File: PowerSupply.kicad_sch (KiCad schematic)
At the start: 42 parts, among them Q1 CSD17318Q2, Q2 CSD17318Q2, U1 TPS55288RPMR

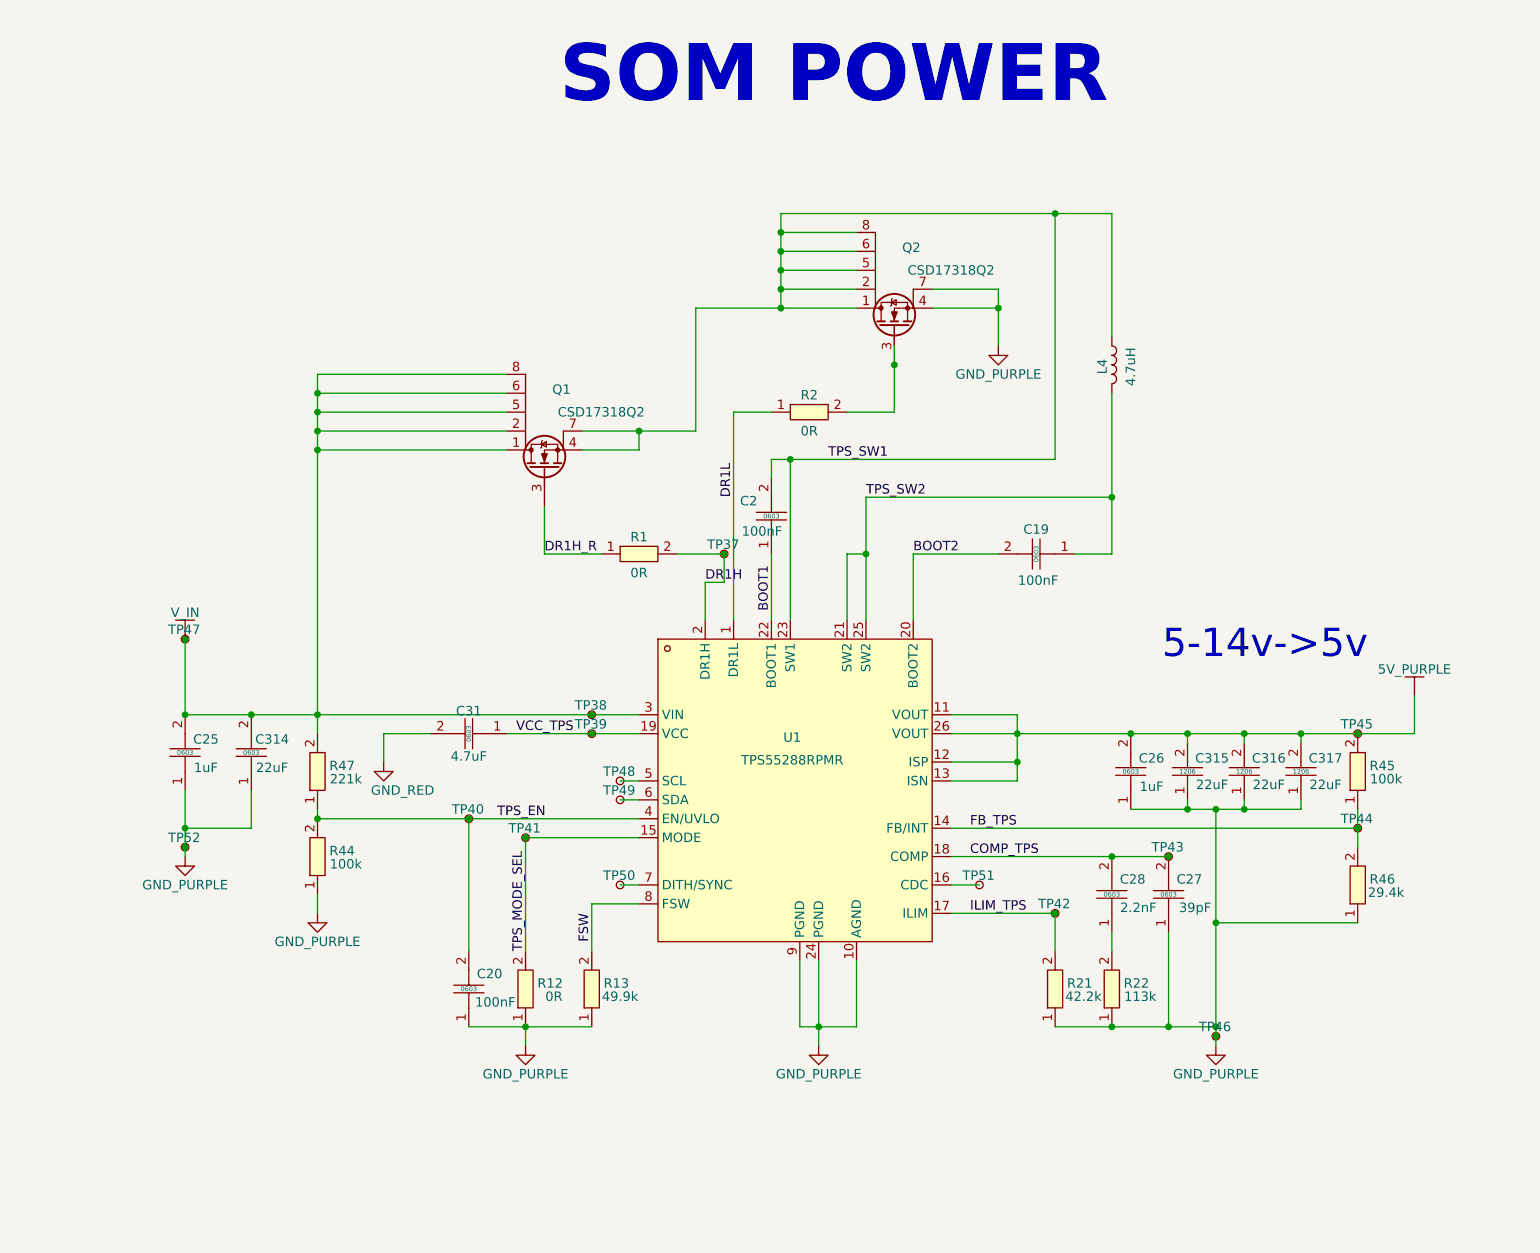
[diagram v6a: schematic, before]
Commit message: Recreate TPS block in KiCad with 0603+ components
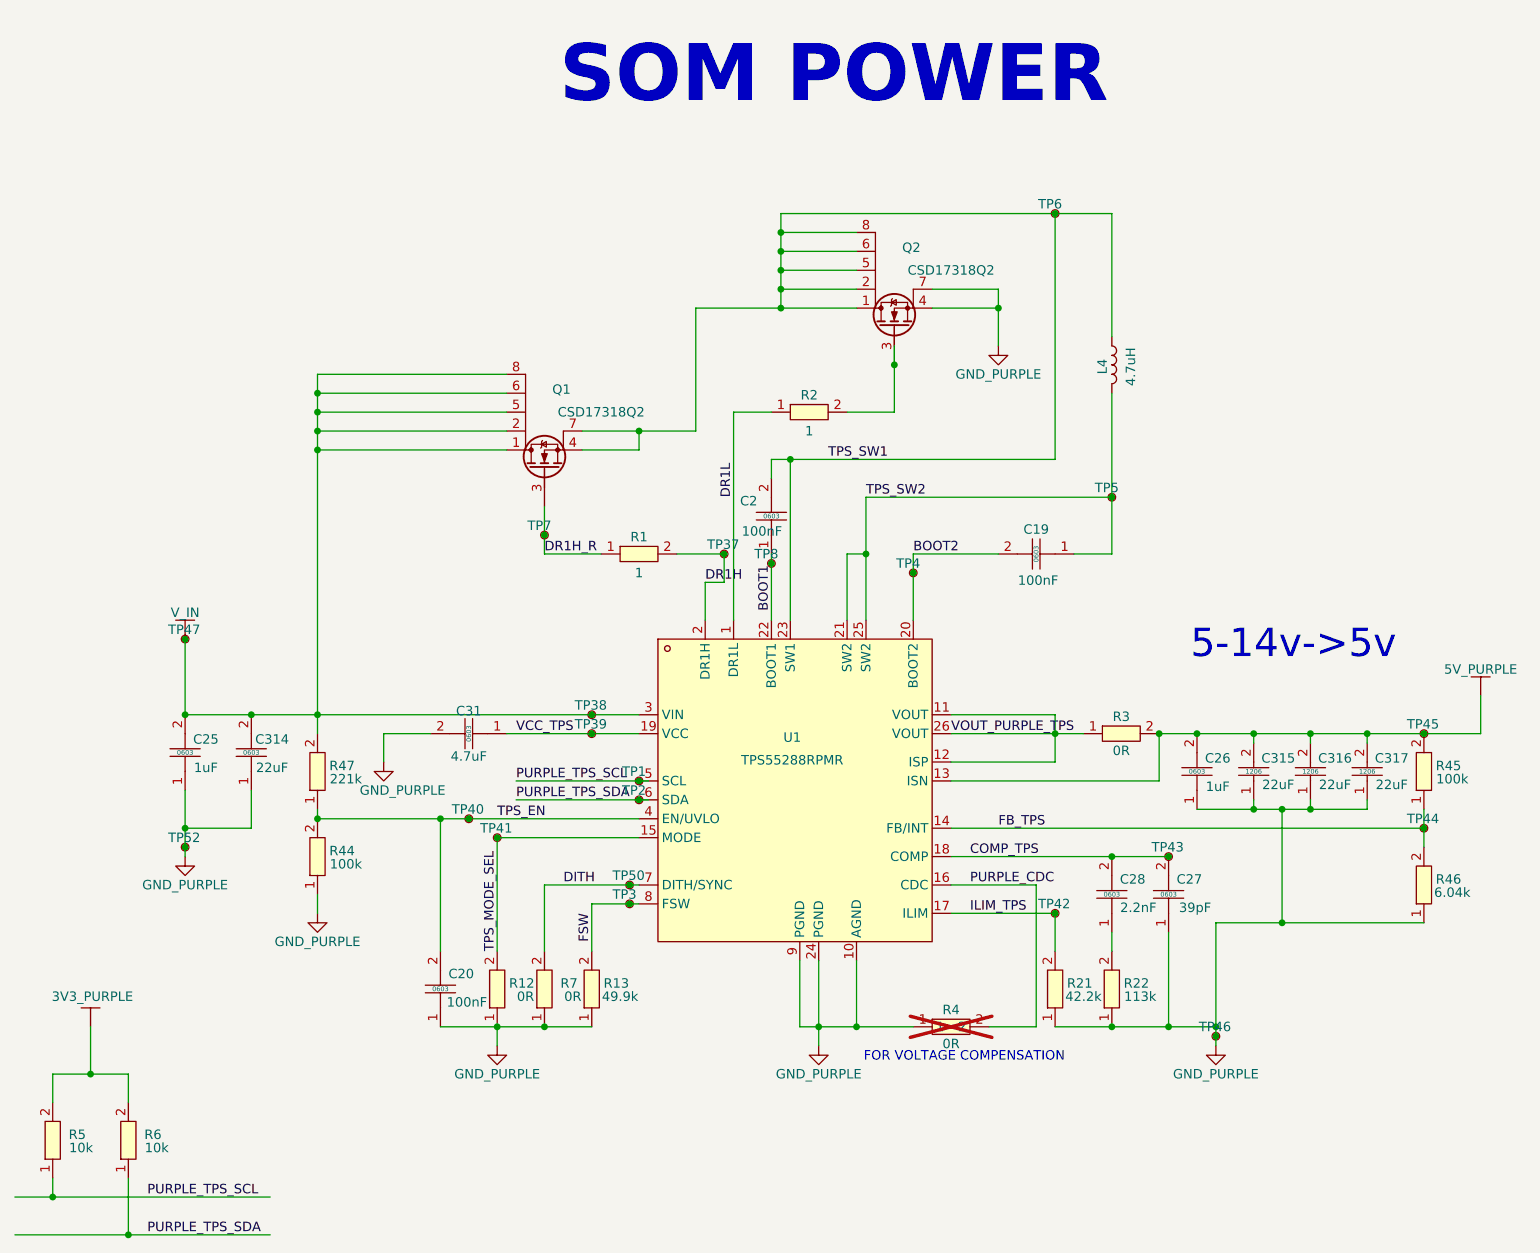
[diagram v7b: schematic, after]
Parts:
- removed TP48, TP49, TP51: TestPoint_Small, symbol Connector:TestPoint_Small
- added R3, R4, R7: RC0603JR-070RL, easyeda2kicad:R0603, symbol easyeda2kicad:0603WAF1003T5E
- added R5, R6: RC0603FR-0710KL, easyeda2kicad:R0603, symbol easyeda2kicad:0603WAF1003T5E
- added TP1, TP2, TP3, TP4, TP5, TP6, TP7, TP8: TestPoint_Small, symbol Connector:TestPoint_Small
- R1, R2: value RC0603JR-070RL -> FRC0603J1R0 TS; Field6 0R -> 1; LCSC Part C95177 -> C2907116
- R46: value FRC0603F2942TS -> FRC0603F6041TS; Field6 29.4k -> 6.04k; LCSC Part C2930086 -> C2999565
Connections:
- net GND_RED is gone; now on net GND_PURPLE: C31.2
- net +5V: now also R3.2; no longer U1.11 (VOUT), U1.12 (ISP), U1.26 (VOUT)
- net BOOT1: now also TP8.1
- net BOOT2: now also TP4.1
- net DR1H_R: now also TP7.1
- net FSW: now also TP3.1
- net GND_PURPLE: now also R4.1, R7.1
- net TPS_SW1: now also TP6.1
- net TPS_SW2: now also TP5.1
- net DITH: now reaches TP50.1, U1.7 (DITH/SYNC)
- net DITH: now also R7.2
- net PURPLE_CDC: now reaches U1.16 (CDC)
- net PURPLE_CDC: now also R4.2
- net PURPLE_TPS_SCL: now reaches U1.5 (SCL)
- net PURPLE_TPS_SCL: now also R5.1, TP1.1
- net PURPLE_TPS_SDA: now reaches U1.6 (SDA)
- net PURPLE_TPS_SDA: now also R6.1, TP2.1
- new net 3V3_PURPLE: R5.2, R6.2
- new net VOUT_PURPLE_TPS: R3.1, U1.11 (VOUT), U1.12 (ISP), U1.26 (VOUT)
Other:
- note added: "FOR VOLTAGE COMPENSATION"
- moved on the sheet: C20, C26, C315, C316, C317, R12, R45, R46, TP41, TP44, TP45, TP50

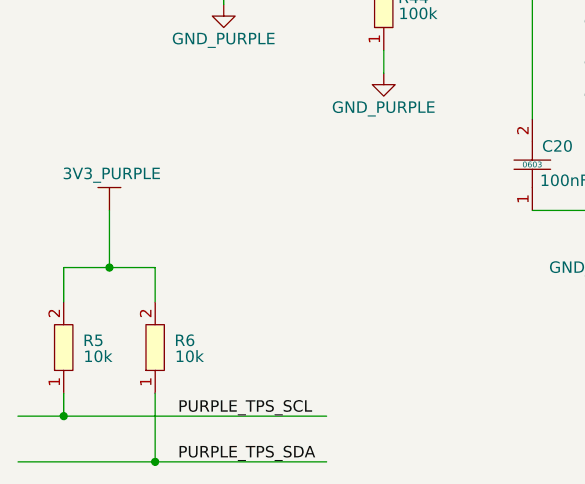
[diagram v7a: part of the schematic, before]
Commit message: Recreate TPS block in KiCad with 0603+ components
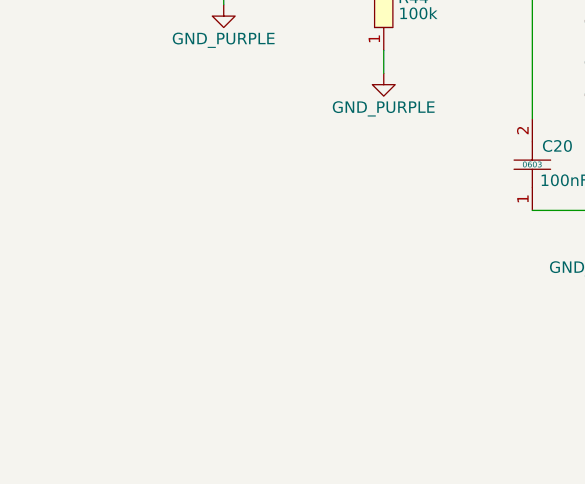
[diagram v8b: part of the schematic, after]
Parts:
- removed R5, R6: RC0603FR-0710KL, easyeda2kicad:R0603, symbol easyeda2kicad:0603WAF1003T5E
